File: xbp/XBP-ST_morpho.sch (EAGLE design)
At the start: 4 parts

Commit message: XBX ST morpho Adapter version 1.0
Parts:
- removed JP6: VCCDin, pinhead:PINHD-1X1
- added JP1: (no value), pinhead:PINHD-2X10
- JP3: value (none) -> VCCDin; device pinhead:PINHD-2X10 -> pinhead:PINHD-1X1
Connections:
- net GND: now also JP1.19, JP1.20, JP1.8, JP4.20; no longer JP3.8
- net N$6: now also JP1.16, JP2.4, JP3.1; no longer JP3.16, JP6.1
- net RSTD: now also JP1.14; no longer JP3.14
- net VCCD: now also JP1.5; no longer JP3.5
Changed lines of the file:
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@@
 <?xml version="1.0" encoding="utf-8"?>
 <!DOCTYPE eagle SYSTEM "eagle.dtd">
-<eagle version="7.4.0">
+<eagle version="7.2.0">
 <drawing>
 <settings>
@@
 <part name="FRAME1" library="frames" deviceset="LETTER_L" device="" value="XBP"/>
 <part name="JP2" library="pinhead" deviceset="PINHD-2X4" device="/90" value="XBD"/>
-<part name="SUPPLY9" library="supply2" deviceset="GND" device=""/>
-<part name="SUPPLY10" library="supply2" deviceset="GND" device=""/>
-<part name="JP3" library="pinhead" deviceset="PINHD-2X10" device=""/>
+<part name="SUPPLY1" library="supply2" deviceset="GND" device=""/>
+<part name="SUPPLY3" library="supply2" deviceset="GND" device=""/>
+<part name="JP1" library="pinhead" deviceset="PINHD-2X10" device=""/>
 <part name="JP4" library="pinhead" deviceset="PINHD-2X10" device=""/>
-<part name="JP6" library="pinhead" deviceset="PINHD-1X1" device="" value="VCCDin"/>
-<part name="SUPPLY13" library="supply2" deviceset="GND" device=""/>
+<part name="JP3" library="pinhead" deviceset="PINHD-1X1" device="" value="VCCDin"/>
+<part name="SUPPLY4" library="supply2" deviceset="GND" device=""/>
+<part name="SUPPLY2" library="supply2" deviceset="GND" device=""/>
+<part name="SUPPLY5" library="supply2" deviceset="GND" device=""/>
 </parts>
 <sheets>
@@
 <instance part="FRAME1" gate="G$2" x="147.32" y="0"/>
 <instance part="JP2" gate="A" x="20.32" y="114.3"/>
-<instance part="SUPPLY9" gate="GND" x="10.16" y="104.14"/>
-<instance part="SUPPLY10" gate="GND" x="35.56" y="124.46"/>
-<instance part="JP3" gate="A" x="20.32" y="162.56"/>
+<instance part="SUPPLY1" gate="GND" x="10.16" y="104.14"/>
+<instance part="SUPPLY3" gate="GND" x="35.56" y="124.46"/>
+<instance part="JP1" gate="A" x="20.32" y="162.56"/>
 <instance part="JP4" gate="A" x="96.52" y="162.56"/>
-<instance part="JP6" gate="G$1" x="40.64" y="144.78"/>
-<instance part="SUPPLY13" gate="GND" x="66.04" y="160.02"/>
+<instance part="JP3" gate="G$1" x="40.64" y="144.78"/>
+<instance part="SUPPLY4" gate="GND" x="66.04" y="160.02"/>
+<instance part="SUPPLY2" gate="GND" x="12.7" y="142.24"/>
+<instance part="SUPPLY5" gate="GND" x="109.22" y="144.78"/>
 </instances>
 <busses>
@@
 <net name="GND" class="0">
 <segment>
-<pinref part="SUPPLY9" gate="GND" pin="GND"/>
+<pinref part="SUPPLY1" gate="GND" pin="GND"/>
 <pinref part="JP2" gate="A" pin="7"/>
 <wire x1="17.78" y1="111.76" x2="10.16" y2="111.76" width="0.1524" layer="91"/>
@@
 <segment>
 <pinref part="JP2" gate="A" pin="2"/>
-<pinref part="SUPPLY10" gate="GND" pin="GND"/>
+<pinref part="SUPPLY3" gate="GND" pin="GND"/>
 <wire x1="30.48" y1="127" x2="35.56" y2="127" width="0.1524" layer="91"/>
 <wire x1="25.4" y1="119.38" x2="30.48" y2="119.38" width="0.1524" layer="91"/>
@@
 </segment>
 <segment>
-<pinref part="JP3" gate="A" pin="8"/>
+<pinref part="JP1" gate="A" pin="8"/>
 <wire x1="25.4" y1="165.1" x2="66.04" y2="165.1" width="0.1524" layer="91"/>
 <wire x1="66.04" y1="165.1" x2="66.04" y2="162.56" width="0.1524" layer="91"/>
-<pinref part="SUPPLY13" gate="GND" pin="GND"/>
+<pinref part="SUPPLY4" gate="GND" pin="GND"/>
 <pinref part="JP4" gate="A" pin="9"/>
 <wire x1="93.98" y1="162.56" x2="66.04" y2="162.56" width="0.1524" layer="91"/>
 <junction x="66.04" y="162.56"/>
+</segment>
+<segment>
+<pinref part="JP1" gate="A" pin="19"/>
+<wire x1="17.78" y1="149.86" x2="12.7" y2="149.86" width="0.1524" layer="91"/>
+<wire x1="12.7" y1="149.86" x2="12.7" y2="144.78" width="0.1524" layer="91"/>
+<pinref part="SUPPLY2" gate="GND" pin="GND"/>
+<pinref part="JP1" gate="A" pin="20"/>
+<wire x1="25.4" y1="149.86" x2="27.94" y2="149.86" width="0.1524" layer="91"/>
+<wire x1="27.94" y1="149.86" x2="27.94" y2="144.78" width="0.1524" layer="91"/>
+<wire x1="27.94" y1="144.78" x2="12.7" y2="144.78" width="0.1524" layer="91"/>
+<junction x="12.7" y="144.78"/>
+</segment>
+<segment>
+<pinref part="JP4" gate="A" pin="20"/>
+<wire x1="101.6" y1="149.86" x2="109.22" y2="149.86" width="0.1524" layer="91"/>
+<wire x1="109.22" y1="149.86" x2="109.22" y2="147.32" width="0.1524" layer="91"/>
+<pinref part="SUPPLY5" gate="GND" pin="GND"/>
 </segment>
 </net>
@@
 <wire x1="45.72" y1="111.76" x2="25.4" y2="111.76" width="0.1524" layer="91"/>
 <label x="25.4" y="111.76" size="1.778" layer="95"/>
-<pinref part="JP3" gate="A" pin="14"/>
+<pinref part="JP1" gate="A" pin="14"/>
 <wire x1="25.4" y1="157.48" x2="45.72" y2="157.48" width="0.1524" layer="91"/>
 </segment>
@@
 <wire x1="17.78" y1="119.38" x2="10.16" y2="119.38" width="0.1524" layer="91"/>
 <label x="7.62" y="144.78" size="1.778" layer="95" rot="R270"/>
-<pinref part="JP3" gate="A" pin="5"/>
+<pinref part="JP1" gate="A" pin="5"/>
 <wire x1="17.78" y1="167.64" x2="10.16" y2="167.64" width="0.1524" layer="91"/>
 <wire x1="10.16" y1="167.64" x2="10.16" y2="119.38" width="0.1524" layer="91"/>
@@
 <net name="N$6" class="0">
 <segment>
-<pinref part="JP6" gate="G$1" pin="1"/>
+<pinref part="JP3" gate="G$1" pin="1"/>
 <wire x1="38.1" y1="144.78" x2="33.02" y2="144.78" width="0.1524" layer="91"/>
 <wire x1="33.02" y1="144.78" x2="33.02" y2="154.94" width="0.1524" layer="91"/>
 <wire x1="33.02" y1="154.94" x2="25.4" y2="154.94" width="0.1524" layer="91"/>
-<pinref part="JP3" gate="A" pin="16"/>
-</segment>
-</net>
+<pinref part="JP1" gate="A" pin="16"/>
+<pinref part="JP2" gate="A" pin="4"/>
+<wire x1="25.4" y1="116.84" x2="38.1" y2="116.84" width="0.1524" layer="91"/>
+<wire x1="40.64" y1="116.84" x2="38.1" y2="116.84" width="0.1524" layer="91"/>
+<wire x1="38.1" y1="116.84" x2="38.1" y2="139.7" width="0.1524" layer="91"/>
+<wire x1="38.1" y1="139.7" x2="33.02" y2="139.7" width="0.1524" layer="91"/>
+<wire x1="33.02" y1="139.7" x2="33.02" y2="144.78" width="0.1524" layer="91"/>
+<junction x="33.02" y="144.78"/>
+</segment>
+</net>

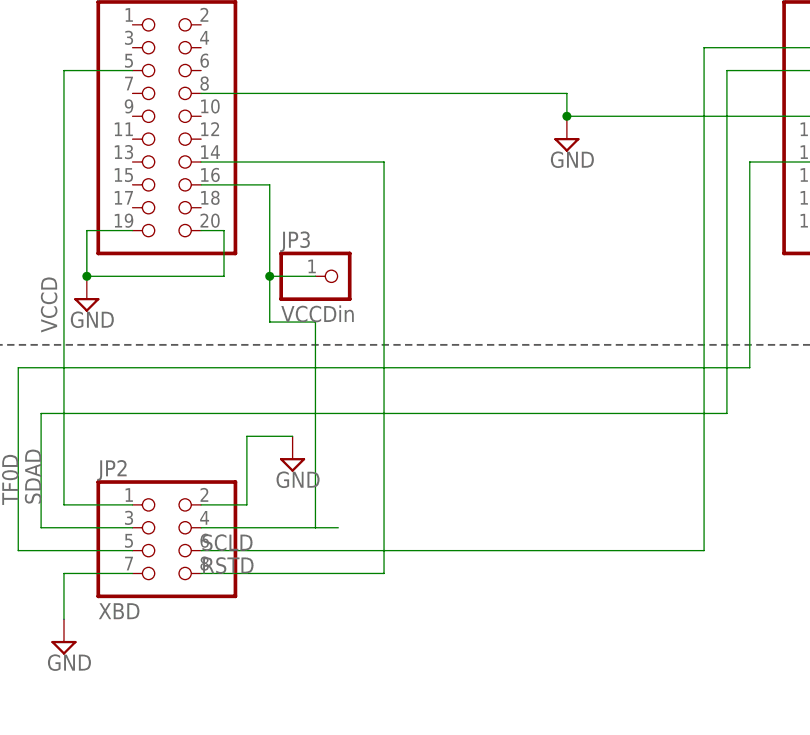
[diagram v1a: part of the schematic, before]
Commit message: SCL was not connected to ST Morpho Pin
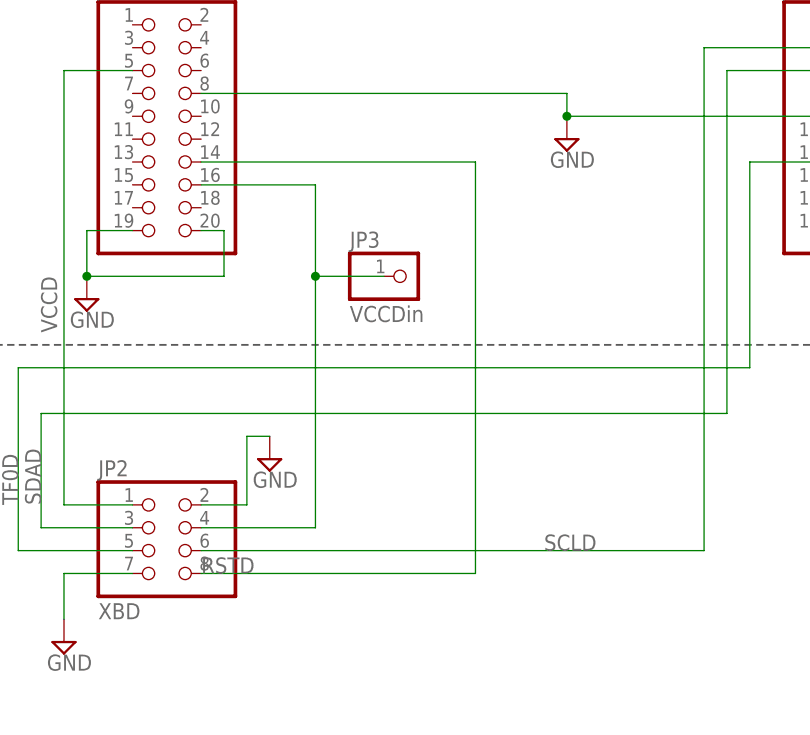
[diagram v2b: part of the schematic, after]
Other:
- note added: "rev 1.1"
- note removed: "rev 1.0"
- moved on the sheet: JP3
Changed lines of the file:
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@@
 <text x="149.86" y="30.48" size="3.81" layer="121">XXBX: XBP - ST morpho Adapter</text>
 <text x="149.86" y="25.4" size="2.54" layer="121">cryptography.gmu.edu</text>
-<text x="236.22" y="7.62" size="2.54" layer="121">rev 1.0</text>
+<text x="236.22" y="7.62" size="2.54" layer="121">rev 1.1</text>
 </plain>
 <instances>
@@
 <instance part="JP2" gate="A" x="20.32" y="114.3"/>
 <instance part="SUPPLY1" gate="GND" x="10.16" y="104.14"/>
-<instance part="SUPPLY3" gate="GND" x="35.56" y="124.46"/>
+<instance part="SUPPLY3" gate="GND" x="33.02" y="124.46"/>
 <instance part="JP1" gate="A" x="20.32" y="162.56"/>
 <instance part="JP4" gate="A" x="96.52" y="162.56"/>
-<instance part="JP3" gate="G$1" x="40.64" y="144.78"/>
+<instance part="JP3" gate="G$1" x="48.26" y="144.78"/>
 <instance part="SUPPLY4" gate="GND" x="66.04" y="160.02"/>
 <instance part="SUPPLY2" gate="GND" x="12.7" y="142.24"/>
@@
 <pinref part="JP2" gate="A" pin="2"/>
 <pinref part="SUPPLY3" gate="GND" pin="GND"/>
-<wire x1="30.48" y1="127" x2="35.56" y2="127" width="0.1524" layer="91"/>
+<wire x1="30.48" y1="127" x2="33.02" y2="127" width="0.1524" layer="91"/>
 <wire x1="25.4" y1="119.38" x2="30.48" y2="119.38" width="0.1524" layer="91"/>
 <wire x1="30.48" y1="119.38" x2="30.48" y2="127" width="0.1524" layer="91"/>
@@
 <pinref part="JP2" gate="A" pin="6"/>
 <wire x1="25.4" y1="114.3" x2="81.28" y2="114.3" width="0.1524" layer="91"/>
-<label x="25.4" y="114.3" size="1.778" layer="95"/>
+<label x="63.5" y="114.3" size="1.778" layer="95"/>
 <pinref part="JP4" gate="A" pin="3"/>
 <wire x1="93.98" y1="170.18" x2="81.28" y2="170.18" width="0.1524" layer="91"/>
@@
 <segment>
 <pinref part="JP2" gate="A" pin="8"/>
-<wire x1="45.72" y1="157.48" x2="45.72" y2="111.76" width="0.1524" layer="91"/>
-<wire x1="45.72" y1="111.76" x2="25.4" y2="111.76" width="0.1524" layer="91"/>
+<wire x1="55.88" y1="157.48" x2="55.88" y2="111.76" width="0.1524" layer="91"/>
+<wire x1="55.88" y1="111.76" x2="25.4" y2="111.76" width="0.1524" layer="91"/>
 <label x="25.4" y="111.76" size="1.778" layer="95"/>
 <pinref part="JP1" gate="A" pin="14"/>
-<wire x1="25.4" y1="157.48" x2="45.72" y2="157.48" width="0.1524" layer="91"/>
+<wire x1="25.4" y1="157.48" x2="55.88" y2="157.48" width="0.1524" layer="91"/>
 </segment>
 </net>
@@
 <segment>
 <pinref part="JP3" gate="G$1" pin="1"/>
-<wire x1="38.1" y1="144.78" x2="33.02" y2="144.78" width="0.1524" layer="91"/>
-<wire x1="33.02" y1="144.78" x2="33.02" y2="154.94" width="0.1524" layer="91"/>
-<wire x1="33.02" y1="154.94" x2="25.4" y2="154.94" width="0.1524" layer="91"/>
+<wire x1="45.72" y1="144.78" x2="38.1" y2="144.78" width="0.1524" layer="91"/>
+<wire x1="38.1" y1="144.78" x2="38.1" y2="154.94" width="0.1524" layer="91"/>
+<wire x1="38.1" y1="154.94" x2="25.4" y2="154.94" width="0.1524" layer="91"/>
 <pinref part="JP1" gate="A" pin="16"/>
 <pinref part="JP2" gate="A" pin="4"/>
 <wire x1="25.4" y1="116.84" x2="38.1" y2="116.84" width="0.1524" layer="91"/>
-<wire x1="40.64" y1="116.84" x2="38.1" y2="116.84" width="0.1524" layer="91"/>
-<wire x1="38.1" y1="116.84" x2="38.1" y2="139.7" width="0.1524" layer="91"/>
-<wire x1="38.1" y1="139.7" x2="33.02" y2="139.7" width="0.1524" layer="91"/>
-<wire x1="33.02" y1="139.7" x2="33.02" y2="144.78" width="0.1524" layer="91"/>
-<junction x="33.02" y="144.78"/>
+<wire x1="38.1" y1="116.84" x2="38.1" y2="144.78" width="0.1524" layer="91"/>
+<junction x="38.1" y="144.78"/>
 </segment>
 </net>
@@
 </sheet>
 </sheets>
-<errors>
-</errors>
 </schematic>
 </drawing>
